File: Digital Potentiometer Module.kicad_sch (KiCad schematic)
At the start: 20 parts, among them J1 Barrel_Jack (>5V), J2 Conn_01x04_Pin, J4 Conn_01x03_Pin, J5 Conn_01x03_Pin, SW1 SW_SPST, SW2 SW_SPST, U1 ESP32-WROOM-32E, U2 AD5231BRUZ10, U3 LM317_SOT-223

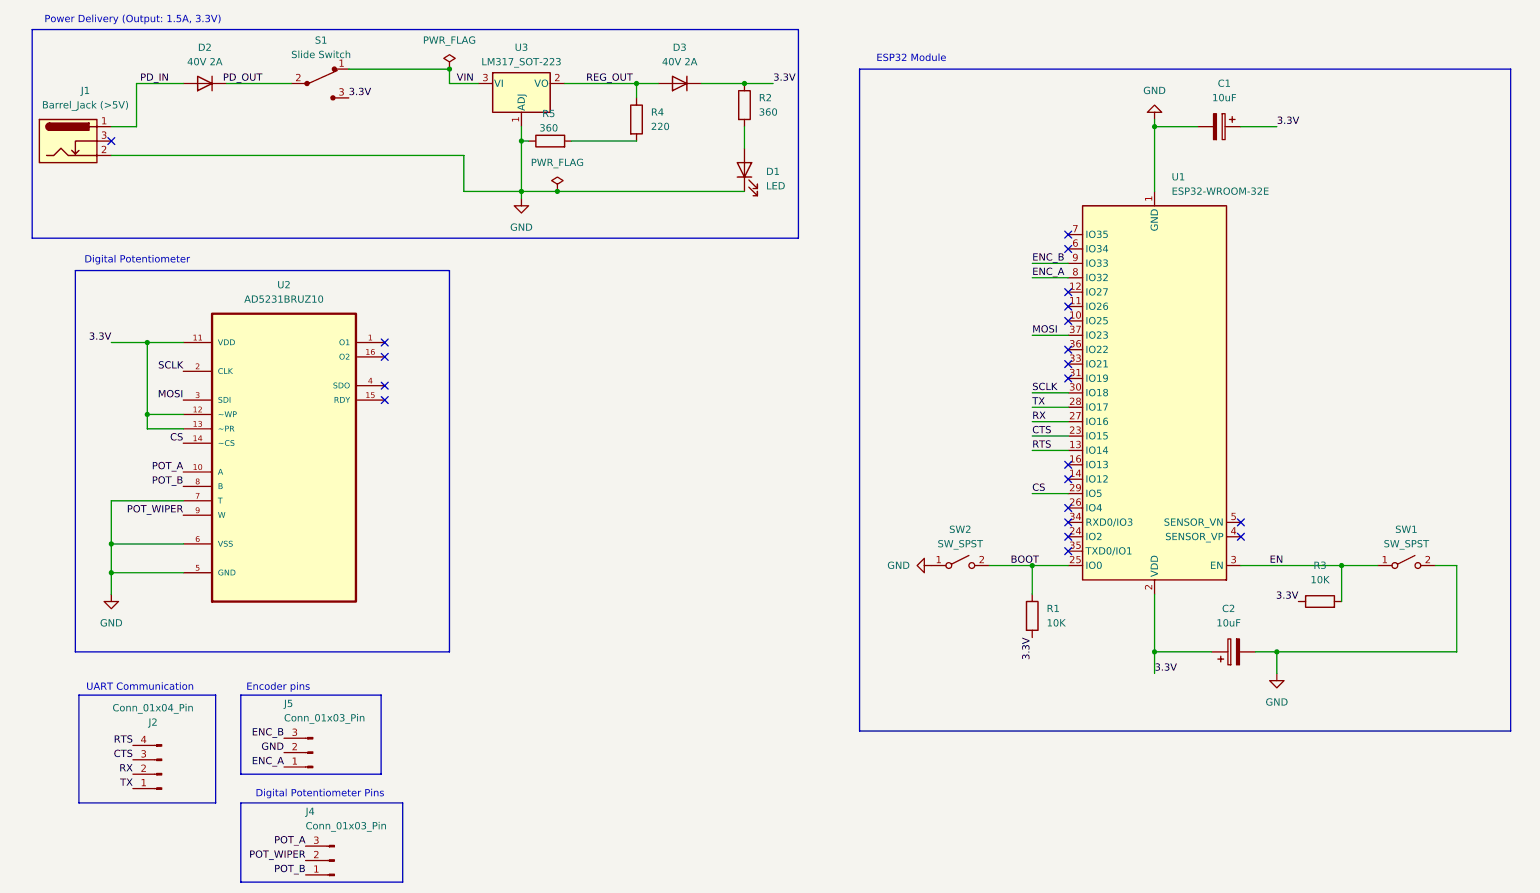
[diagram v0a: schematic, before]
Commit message: fix UART communication pins
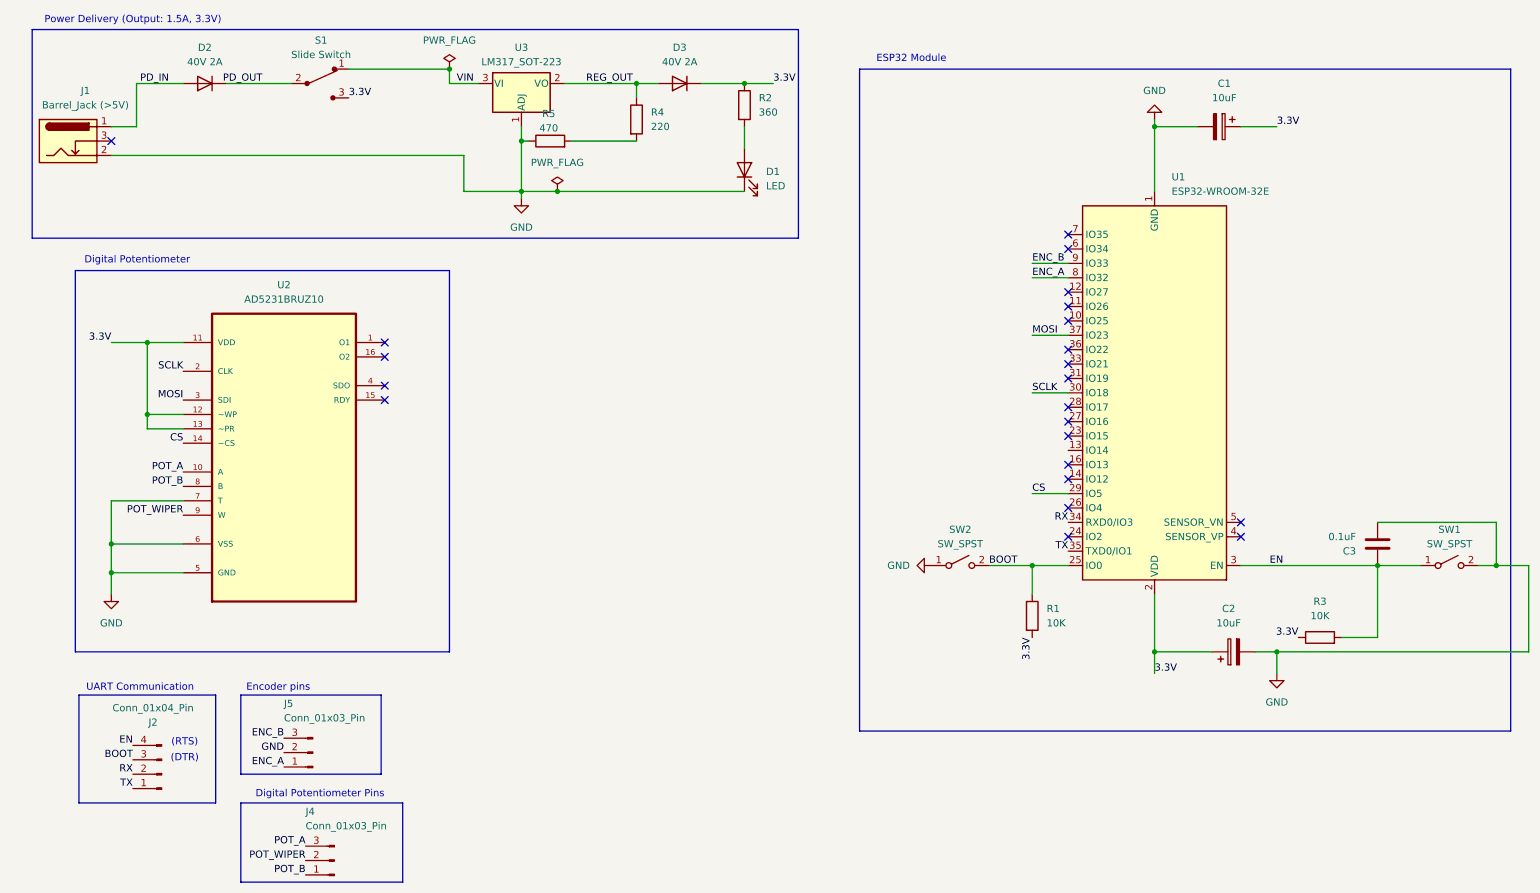
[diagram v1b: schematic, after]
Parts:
- added C3: 0.1uF, Capacitor_SMD:C_1206_3216Metric, symbol Device:C
- R5: value 360 -> 470
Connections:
- net BOOT: now also J2.3 (Pin_3)
- net EN: now also J2.4 (Pin_4), C3.2
- net GND: now also C3.1
- net RX: now also U1.34 (RXD0/IO3); no longer U1.27 (IO16)
- net TX: now also U1.35 (TXD0/IO1); no longer U1.28 (IO17)
- net CTS: no longer names the net of U1.23 (IO15)
- net CTS: no longer J2.3 (Pin_3)
- net RTS: no longer names the net of U1.13 (IO14)
- net RTS: no longer J2.4 (Pin_4)
- no-connect marks 21 -> 22
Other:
- note added: "(DTR)"
- note added: "(RTS)"
- moved on the sheet: R3, SW1

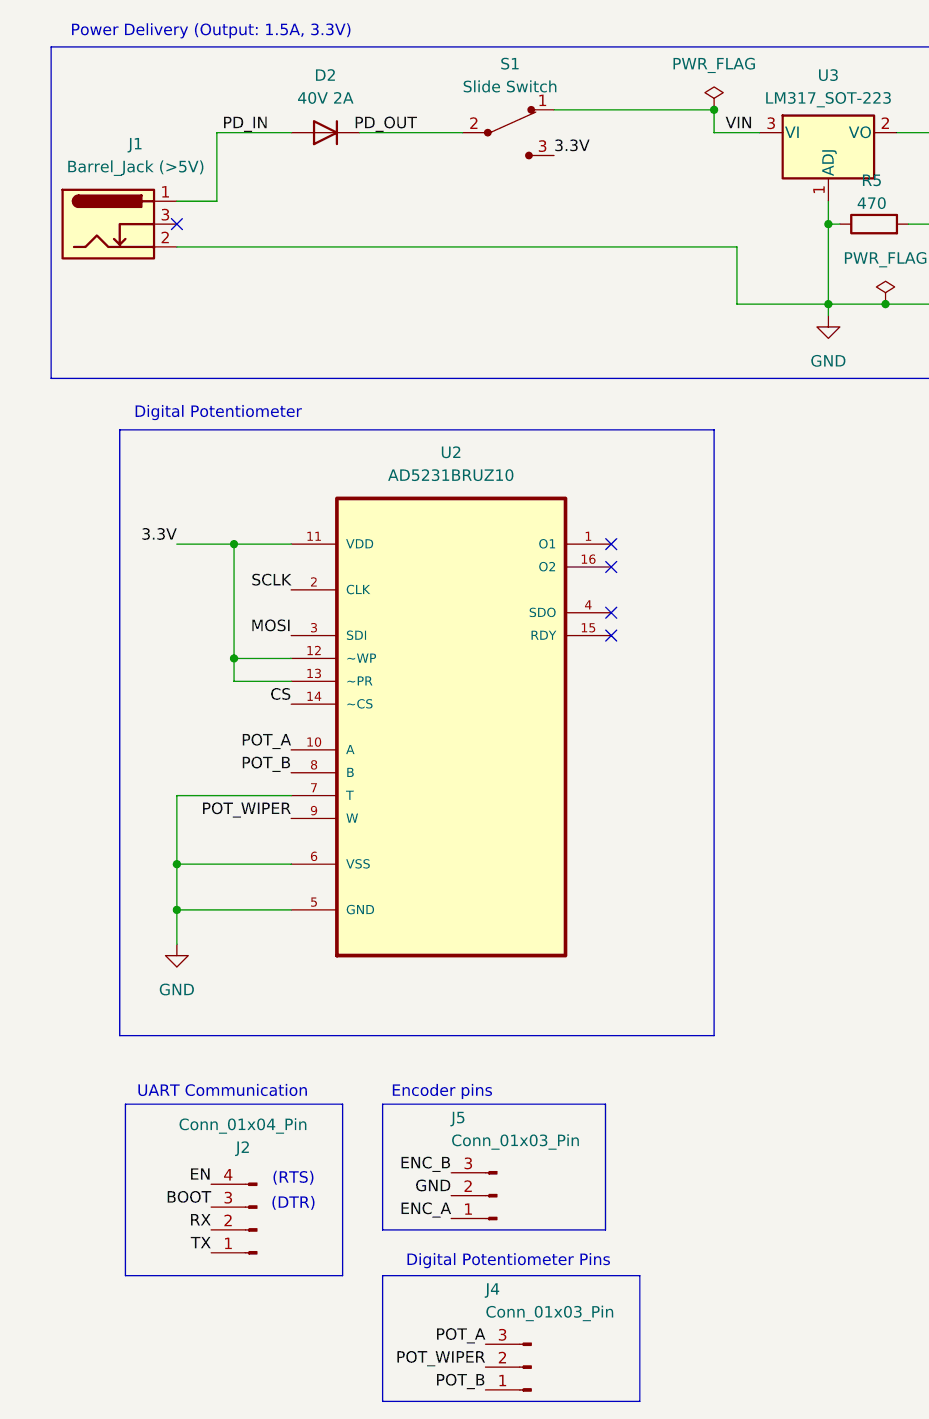
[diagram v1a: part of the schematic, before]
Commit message: add vcc, gnd pins. change dtr pin to cts
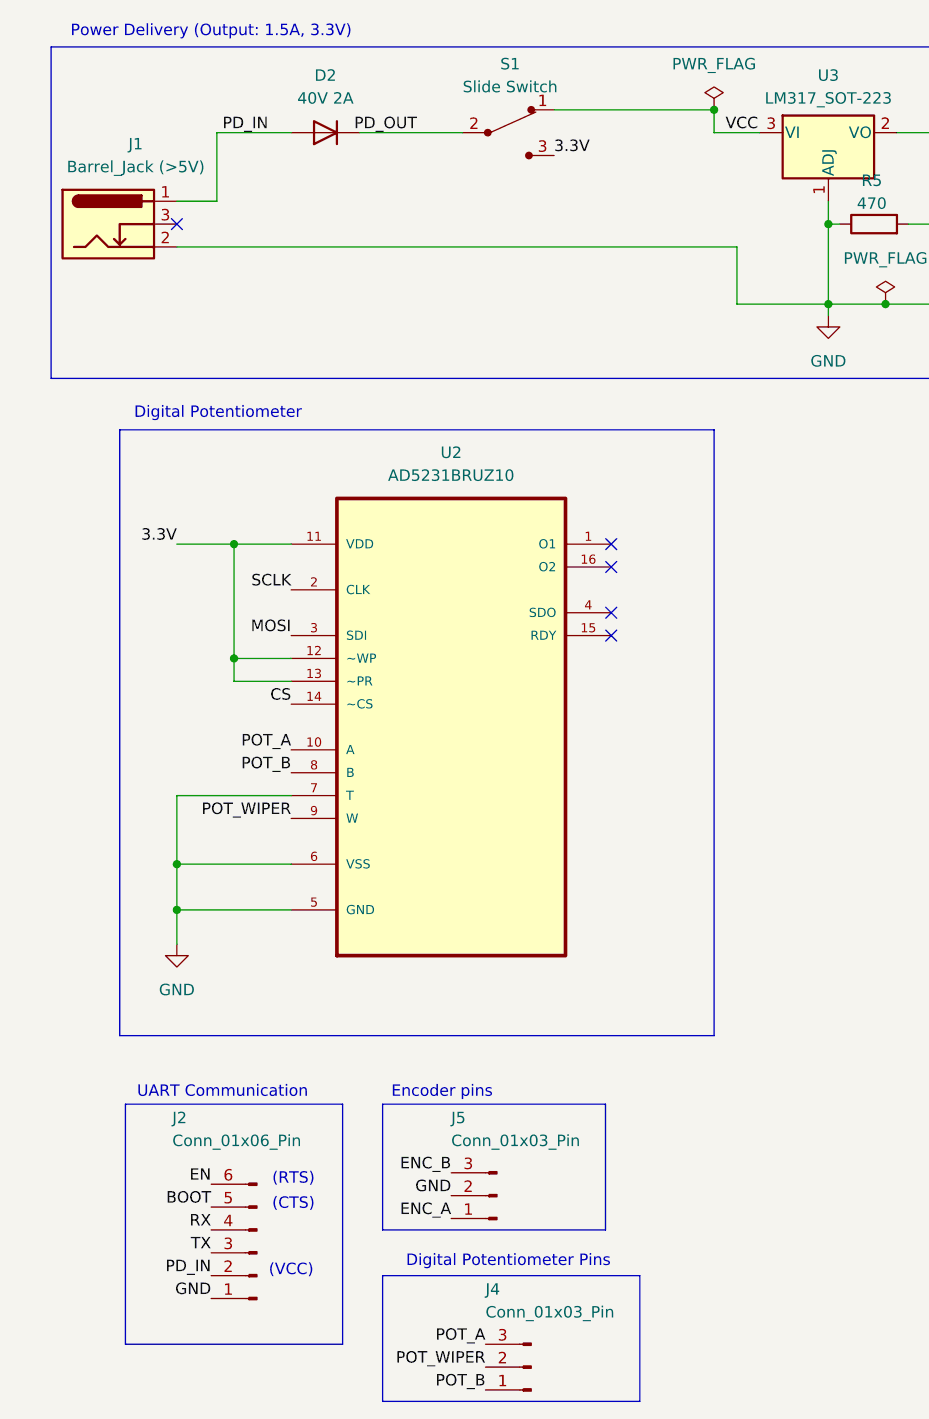
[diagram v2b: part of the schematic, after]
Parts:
- removed J2: Conn_01x04_Pin, Connector_PinHeader_2.54mm:PinHeader_1x04_P2.54mm_Vertical, symbol Connector:Conn_01x04_Pin
- added J2: Conn_01x06_Pin, Connector_PinHeader_2.54mm:PinHeader_1x06_P2.54mm_Vertical, symbol Connector:Conn_01x06_Pin
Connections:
- net BOOT: now also J2.5 (Pin_5)
- net EN: now also J2.6 (Pin_6)
- net GND: now also J2.1 (Pin_1)
- net PD_IN: now also J2.2 (Pin_2)
- net RX: now also J2.4 (Pin_4)
- net TX: now also J2.3 (Pin_3)
- net VIN renamed VCC
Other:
- note added: "(CTS)"
- note added: "(VCC)"
- note removed: "(DTR)"
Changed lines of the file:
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@@
 	(rectangle
 		(start 23.495 138.43)
-		(end 47.625 157.48)
+		(end 47.625 165.1)
 		(stroke
 			(width 0)
@@
 		)
 	)
-	(text "(DTR)"
+	(text "(CTS)"
 		(exclude_from_sim no)
 		(at 42.164 149.606 0)
@@
 		(exclude_from_sim no)
 		(at 34.29 137.16 0)
+		(effects
+			(font
+				(size 1.27 1.27)
+			)
+		)
+	)
+	(text "(VCC)"
+		(exclude_from_sim no)
+		(at 41.91 156.972 0)
 		(effects
 			(font
@@
 		)
 	)
+	(label "PD_IN"
+		(at 33.02 157.48 180)
+		(fields_autoplaced yes)
+		(effects
+			(font
+				(size 1.27 1.27)
+			)
+			(justify right bottom)
+		)
+	)
 	(label "EN"
 		(at 33.02 147.32 180)
@@
 		)
 	)
+	(label "GND"
+		(at 33.02 160.02 180)
+		(fields_autoplaced yes)
+		(effects
+			(font
+				(size 1.27 1.27)
+			)
+			(justify right bottom)
+		)
+	)
 	(label "POT_WIPER"
 		(at 41.91 106.68 180)
@@
 		)
 	)
-	(label "VIN"
+	(label "VCC"
 		(at 90.17 30.48 0)
 		(fields_autoplaced yes)
@@
 	)
 	(symbol
+		(lib_id "Connector:Conn_01x06_Pin")
+		(at 38.1 154.94 180)
+		(unit 1)
+		(exclude_from_sim no)
+		(in_bom yes)
+		(on_board yes)
+		(dnp no)
+		(property "Reference" "J2"
+			(at 28.702 139.954 0)
+			(effects
+				(font
+					(size 1.27 1.27)
+				)
+				(justify right)
+			)
+		)
+		(property "Value" "Conn_01x06_Pin"
+			(at 28.702 142.494 0)
+			(effects
+				(font
+					(size 1.27 1.27)
+				)
+				(justify right)
+			)
+		)
+		(property "Footprint" "Connector_PinHeader_2.54mm:PinHeader_1x06_P2.54mm_Vertical"
+			(at 38.1 154.94 0)
+			(effects
+				(font
+					(size 1.27 1.27)
+				)
+				(hide yes)
+			)
+		)
+		(property "Datasheet" "~"
+			(at 38.1 154.94 0)
+			(effects
+				(font
+					(size 1.27 1.27)
+				)
+				(hide yes)
+			)
+		)
+		(property "Description" "Generic connector, single row, 01x06, script generated"
+			(at 38.1 154.94 0)
+			(effects
+				(font
+					(size 1.27 1.27)
+				)
+				(hide yes)
+			)
+		)
+		(property "Purpose" ""
+			(at 38.1 154.94 0)
+			(effects
+				(font
+					(size 1.27 1.27)
+				)
+			)
+		)
+		(pin "6"
+		)
+		(pin "4"
+		)
+		(pin "2"
+		)
+		(pin "5"
+		)
+		(pin "1"
+		)
+		(pin "3"
+		)
+		(instances
+			(project ""
+				(path "/f9605a72-0ec6-49c8-8d90-8c2a65c3e011"
+					(reference "J2")
+					(unit 1)
+				)
+			)
+		)
+	)
+	(symbol
 		(lib_id "power:GND")
 		(at 101.6 50.8 0)
@@
 					(unit 1)
 				)
-			)
-		)
-	)
-	(symbol
-		(lib_id "Connector:Conn_01x04_Pin")
-		(at 38.1 152.4 180)
-		(unit 1)
-		(exclude_from_sim no)
-		(in_bom yes)
-		(on_board yes)
-		(dnp no)
-		(property "Reference" "J2"
-			(at 36.576 143.256 0)
-			(effects
-				(font
-					(size 1.27 1.27)
-				)
-			)
-		)
-		(property "Value" "Conn_01x04_Pin"
-			(at 36.576 140.716 0)
-			(effects
-				(font
-					(size 1.27 1.27)
-				)
-			)
-		)
-		(property "Footprint" "Connector_PinHeader_2.54mm:PinHeader_1x04_P2.54mm_Vertical"
-			(at 38.1 152.4 0)
-			(effects
-				(font
-					(size 1.27 1.27)
-				)
-				(hide yes)
-			)
-		)
-		(property "Datasheet" "~"
-			(at 38.1 152.4 0)
-			(effects
-				(font
-					(size 1.27 1.27)
-				)
-				(hide yes)
-			)
-		)
-		(property "Description" "Generic connector, single row, 01x04, script generated"
-			(at 38.1 152.4 0)
-			(effects
-				(font
-					(size 1.27 1.27)
-				)
-				(hide yes)
-			)
-		)
-		(pin "1"
-		)
-		(pin "3"
-		)
-		(pin "4"
-		)
-		(pin "2"
-		)
-		(instances
-			(project ""
-				(path "/f9605a72-0ec6-49c8-8d90-8c2a65c3e011"
-					(reference "J2")
-					(unit 1)
-				)

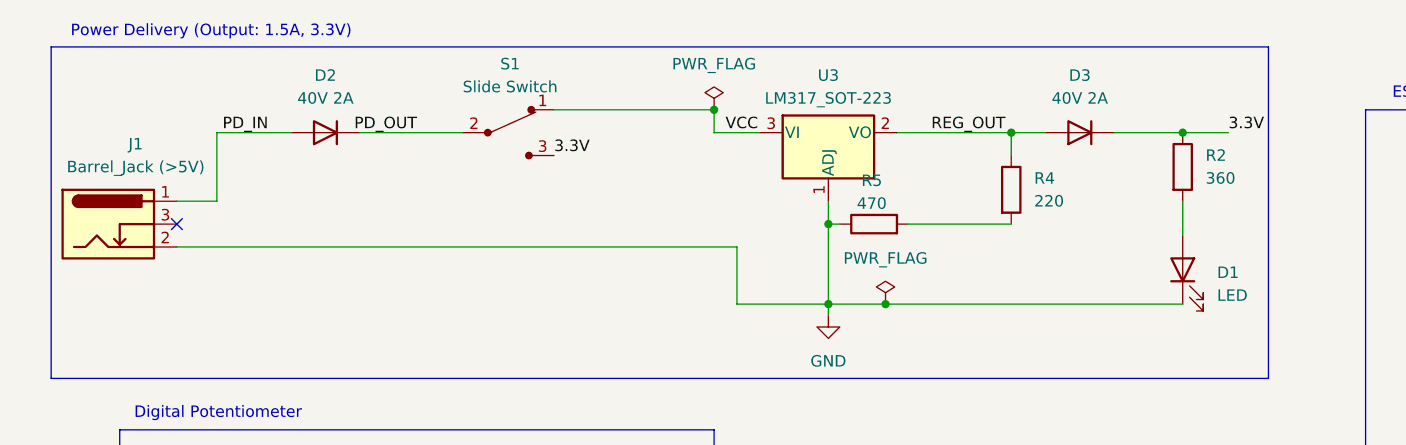
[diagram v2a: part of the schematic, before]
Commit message: fix issues with serial communication pins
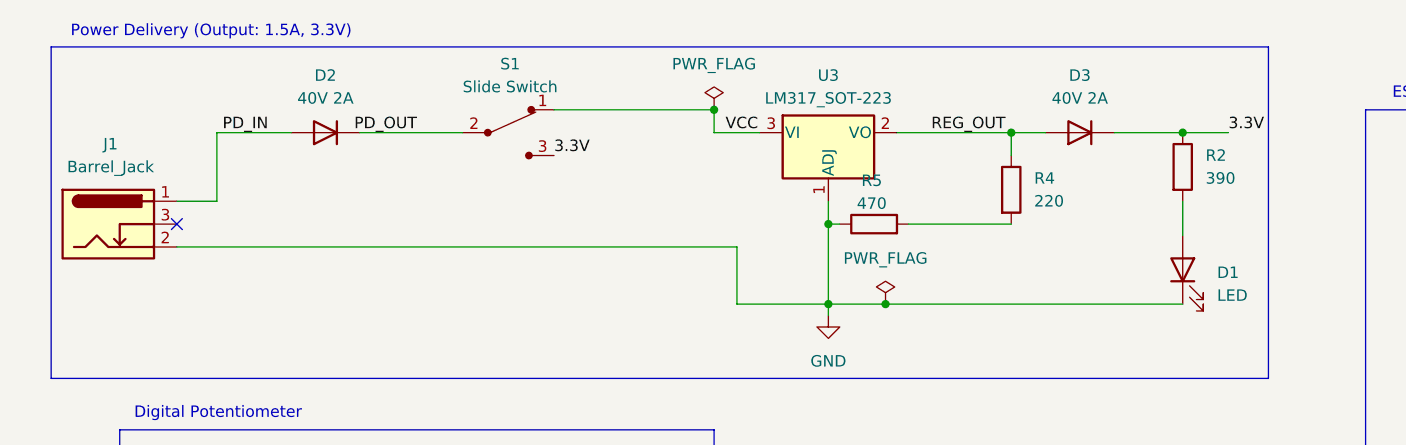
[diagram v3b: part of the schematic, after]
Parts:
- J1: value Barrel_Jack (>5V) -> Barrel_Jack
- R2: value 360 -> 390
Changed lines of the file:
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@@
 			)
 		)
-		(property "Value" "360"
+		(property "Value" "390"
 			(at 143.51 35.5599 0)
 			(effects
@@
 		(dnp no)
 		(property "Reference" "J1"
-			(at 24.638 31.75 0)
-			(effects
-				(font
-					(size 1.27 1.27)
-				)
-			)
-		)
-		(property "Value" "Barrel_Jack (>5V)"
-			(at 24.638 34.29 0)
-			(effects
-				(font
+			(at 21.844 31.75 0)
+			(effects
+				(font
+					(size 1.27 1.27)
+				)
+			)
+		)
+		(property "Value" "Barrel_Jack"
+			(at 21.844 34.29 0)
+			(effects
+				(font

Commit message: improve pcb design
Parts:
- added C4: 0.1uF, Capacitor_SMD:C_1206_3216Metric, symbol Device:C
- C2: value 10uF -> 22uF
- S1: footprint Custom:Switch_Slide_8.5x3.5mm -> Connector_PinHeader_2.54mm:PinHeader_1x03_P2.54mm_Vertical
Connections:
- net 3.3V: now also C4.1
- net GND: now also C4.2
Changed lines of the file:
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@@
 	)
 	(junction
+		(at 231.14 130.81)
+		(diameter 0)
+		(color 0 0 0 0)
+	)
+	(junction
 		(at 213.36 38.1)
 		(diameter 0)
@@
 	)
 	(junction
+		(at 213.36 121.92)
+		(diameter 0)
+		(color 0 0 0 0)
+	)
+	(junction
 		(at 35.56 76.2)
 		(diameter 0)
@@
 	(wire
 		(pts
+			(xy 213.36 121.92) (xy 213.36 130.81)
+		)
+		(stroke
+			(width 0)
+			(type default)
+		)
+	)
+	(wire
+		(pts
 			(xy 71.12 27.94) (xy 88.9 27.94)
 		)
@@
 	(wire
 		(pts
-			(xy 213.36 120.65) (xy 213.36 130.81)
+			(xy 213.36 120.65) (xy 213.36 121.92)
 		)
 		(stroke
@@
 	(wire
 		(pts
+			(xy 231.14 129.54) (xy 231.14 130.81)
+		)
+		(stroke
+			(width 0)
+			(type default)
+		)
+	)
+	(wire
+		(pts
 			(xy 110.49 40.64) (xy 121.92 40.64)
 		)
@@
 	(wire
 		(pts
+			(xy 213.36 121.92) (xy 231.14 121.92)
+		)
+		(stroke
+			(width 0)
+			(type default)
+		)
+	)
+	(wire
+		(pts
 			(xy 234.95 130.81) (xy 234.95 134.62)
 		)
@@
 			)
 		)
-		(property "Footprint" "Custom:Switch_Slide_8.5x3.5mm"
+		(property "Footprint" "Connector_PinHeader_2.54mm:PinHeader_1x03_P2.54mm_Vertical"
 			(at 71.12 25.4 0)
 			(effects
@@
 		(on_board yes)
 		(dnp no)
-		(fields_autoplaced yes)
 		(property "Reference" "C2"
-			(at 226.441 123.19 90)
+			(at 227.33 135.382 90)
 			(effects
 				(font
@@
 			)
 		)
-		(property "Value" "10uF"
-			(at 226.441 125.73 90)
+		(property "Value" "22uF"
+			(at 227.33 137.922 90)
 			(effects
 				(font
@@
 					(unit 1)
 				)
+			)
+		)
+	)
+	(symbol
+		(lib_id "Device:C")
+		(at 231.14 125.73 0)
+		(unit 1)
+		(exclude_from_sim no)
+		(in_bom yes)
+		(on_board yes)
+		(dnp no)
+		(property "Reference" "C4"
+			(at 234.95 123.19 0)
+			(effects
+				(font
+					(size 1.27 1.27)
+				)
+				(justify right)
+			)
+		)
+		(property "Value" "0.1uF"
+			(at 234.95 120.65 0)
+			(effects
+				(font
+					(size 1.27 1.27)
+				)
+				(justify right)
+			)
+		)
+		(property "Footprint" "Capacitor_SMD:C_1206_3216Metric"
+			(at 232.1052 129.54 0)
+			(effects
+				(font
+					(size 1.27 1.27)
+				)
+				(hide yes)
+			)
+		)
+		(property "Datasheet" "~"
+			(at 231.14 125.73 0)
+			(effects
+				(font
+					(size 1.27 1.27)
+				)
+				(hide yes)
+			)
+		)
+		(property "Description" "Unpolarized capacitor"
+			(at 231.14 125.73 0)
+			(effects
+				(font
+					(size 1.27 1.27)
+				)
+				(hide yes)
+			)
+		)
+		(property "Purpose" ""
+			(at 231.14 125.73 0)
+			(effects
+				(font
+					(size 1.27 1.27)
+				)
+			)
+		)
+		(pin "1"
+		)
+		(pin "2"
+		)
+		(instances
+			(project "Digital Potentiometer Module"
+				(path "/f9605a72-0ec6-49c8-8d90-8c2a65c3e011"
+					(reference "C4")
+					(unit 1)
+				)
